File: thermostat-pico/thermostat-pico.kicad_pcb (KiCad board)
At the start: 2 copper layers, 40 x 30 mm, 22 parts, among them J1 VAC IN, J2 CTRL, J3 UART, U1 LY68L6400SLIT, U2 ESP32-PICO-D4, U3 LM358DR2G, U4 TPS5430DDA, U5 TPS5430DDA

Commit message: Should be finished
Maybe the antenna could be different
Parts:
- removed C4: 0.1uF/50V, Capacitor_SMD:C_0603_1608Metric
- added C10: 0.01uF, Capacitor_SMD:C_0402_1005Metric, F.Cu at (107.5, 99.0)
- added C8: 470uF/6.3V, Capacitor_Tantalum_SMD:CP_EIA-7343-31_Kemet-D, F.Cu at (118.0, 101.1)
- added C9: 470uF/6.3V, Capacitor_Tantalum_SMD:CP_EIA-7343-31_Kemet-D, F.Cu at (106.3, 103.5)
- added D2: SS34, Diode_SMD:D_SMA, F.Cu at (128.5, 105.2)
- added D3: SS34, Diode_SMD:D_SMA, F.Cu at (95.0, 112.5)
- added H1: MountingHole_Pad, MountingHole:MountingHole_2.2mm_M2_DIN965_Pad, F.Cu at (85.2, 114.2)
- added H2: MountingHole_Pad, MountingHole:MountingHole_2.2mm_M2_DIN965_Pad, F.Cu at (130.8, 88.8)
- added L1: 22uH, inductors:L_SXN_SMRH74-220MT, F.Cu at (127.5, 95.5)
- added L2: 22uH, inductors:L_SXN_SMRH74-220MT, F.Cu at (105.0, 110.5)
- added R10: 270, Resistor_SMD:R_0603_1608Metric, F.Cu at (114.5, 105.8)
- added R5: 10k, Resistor_SMD:R_0603_1608Metric, F.Cu at (100.0, 101.5)
- added R6: 10k, Resistor_SMD:R_0603_1608Metric, F.Cu at (114.5, 98.7)
- added R7: 1.1k, Resistor_SMD:R_0603_1608Metric, F.Cu at (96.5, 101.5)
- added R8: 5.6k, Resistor_SMD:R_0603_1608Metric, F.Cu at (114.5, 102.3)
- added R9: 33, Resistor_SMD:R_0603_1608Metric, F.Cu at (93.0, 101.5)
- AE1: value Antenna -> Antenna_Shield; footprint RF_Antenna:Texas_SWRA117D_2.4GHz_Right -> RF_Antenna:Texas_SWRA117D_2.4GHz_Left
- C3: value 0.1uF/50V -> 0.1uF; footprint Capacitor_SMD:C_0603_1608Metric -> Capacitor_SMD:C_0402_1005Metric
- C7: value 0.01uF -> 0.1uF
- JP1: moved to B.Cu
- moved J1 43.8 mm to (130.0, 113.5), turned to 180 degrees
- moved C2 31.9 mm to (123.5, 108.5)
- moved R1 27.2 mm to (91.5, 98.0), turned to -90 degrees
- moved J2 27.1 mm to (86.0, 105.2), turned to 90 degrees
- moved C6 26.8 mm to (130.0, 100.2), turned to 0 degrees
- moved D1 25.8 mm to (115.0, 112.5), turned to 180 degrees
- moved R2 23.5 mm to (91.5, 95.6), turned to 90 degrees
- moved U5 21.8 mm to (123.5, 103.5), turned to -90 degrees
- moved U3 20.8 mm to (96.5, 96.6)
- moved C3 16.2 mm to (100.5, 92.0), turned to 0 degrees
- moved R4 16.1 mm to (102.0, 93.7), turned to 90 degrees
- moved R3 13.5 mm to (102.0, 95.8), turned to 90 degrees
- moved J3 12.9 mm to (103.9, 87.5)
- moved U1 11.6 mm to (118.0, 92.0)
- moved U2 11.3 mm to (107.2, 93.5)
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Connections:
- net Net-(C5-Pad2) renamed /PH12
- net Net-(C6-Pad2) renamed /PH33
- AE1 pad 2: (no net) -> GND
- C1 pad 1: /REC_OUT -> /D1_OUT
- C2 pad 1: /REC_OUT -> /D1_OUT
- C3 pad 1: /REC_OUT -> GND
- C3 pad 2: GND -> /ADC1
- D1 pad 3: /REC_OUT -> /D1_OUT
- JP1 pad 1: unconnected-(JP1-Pad1) -> /BOOT
- JP1 pad 2: unconnected-(JP1-Pad2) -> GND
- R3 pad 2: Net-(R3-Pad2) -> /ADC1
- R4 pad 1: Net-(R3-Pad2) -> /ADC1
- U2 pad 1: Net-(U2-Pad1) -> /VCC33
- U2 pad 14: unconnected-(U2-Pad14) -> /DAC1
- U2 pad 15: unconnected-(U2-Pad15) -> /DAC2
- U2 pad 19: unconnected-(U2-Pad19) -> /VCC33
- U2 pad 23: unconnected-(U2-Pad23) -> /BOOT
- U2 pad 3: Net-(U2-Pad3) -> /VCC33
- U2 pad 37: unconnected-(U2-Pad37) -> /VCC33
- U2 pad 4: Net-(U2-Pad3) -> /VCC33
- U2 pad 43: Net-(U2-Pad1) -> /VCC33
- U2 pad 46: Net-(U2-Pad1) -> /VCC33
- U2 pad 5: unconnected-(U2-Pad5) -> /ADC1
- U2 pad 6: unconnected-(U2-Pad6) -> /ADC2
- U3 pad 3: unconnected-(U3-Pad3) -> /DAC1
- U3 pad 4: unconnected-(U3-Pad4) -> GND
- U3 pad 8: unconnected-(U3-Pad8) -> /VCC12
- U4 pad 4: unconnected-(U4-Pad4) -> Net-(R5-Pad2)
- U4 pad 7: /REC_OUT -> /D1_OUT
- U5 pad 4: unconnected-(U5-Pad4) -> Net-(R6-Pad2)
- U5 pad 7: /REC_OUT -> /D1_OUT
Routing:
- net GND: track 0.00 -> 60.1 mm, vias 0 -> 13
- net /VCC33: track 0.00 -> 55.2 mm, vias 0 -> 5
- net /D1_OUT: track 0.00 -> 25.5 mm, vias 0 -> 2
- net /BOOT: track 0.00 -> 16.0 mm, vias 0 -> 1
- net /VCC12: track 0.00 -> 15.0 mm, vias 0 -> 2
- net /CTRL0_IN: track 0.00 -> 14.4 mm
- net /DAC1: track 0.00 -> 11.7 mm
- net /CTRL0_OUT: track 0.00 -> 9.90 mm
- net Net-(R6-Pad2): track 0.00 -> 9.60 mm
- net Net-(R5-Pad2): track 0.00 -> 6.42 mm
- net /ADC1: track 0.00 -> 5.89 mm
- net /24VAC+: track 10.7 -> 5.37 mm
- net /24VAC-: track 9.08 -> 13.7 mm
- net Net-(C6-Pad1): track 0.00 -> 4.34 mm
- net Net-(R3-Pad1): track 0.00 -> 4.23 mm
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- added copper zone on B.Cu, net /D1_OUT
- added copper zone on F.Cu, net /PH12
- added copper zone on F.Cu, net /PH33
- added copper zone on F.Cu, net /VCC12
- added copper zone on F.Cu, net /VCC33
- added copper zone on B.Cu, net GND
- added copper zone on F.Cu, net GND
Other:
- board size 40 x 30 mm -> 50 x 30 mm
- board text added: "+"
- board text added: "-"
- board text added: "24VAC"
- board text added: "CTRL_IN"
- board text added: "CTRL_OUT"
- board text added: "GND"
- board text added: "URX"
- board text added: "UTX"
- board text added: "VCC"

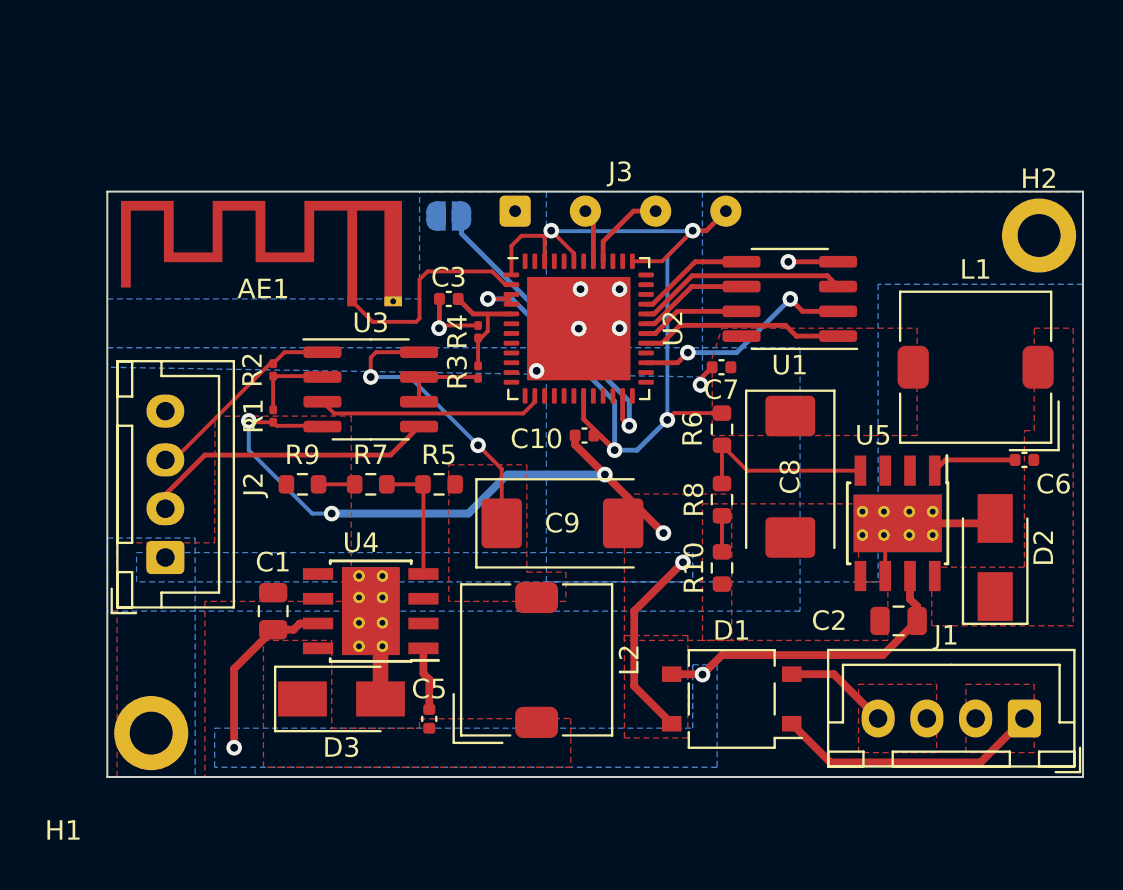
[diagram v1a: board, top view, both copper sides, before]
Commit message: Added slow start circuit
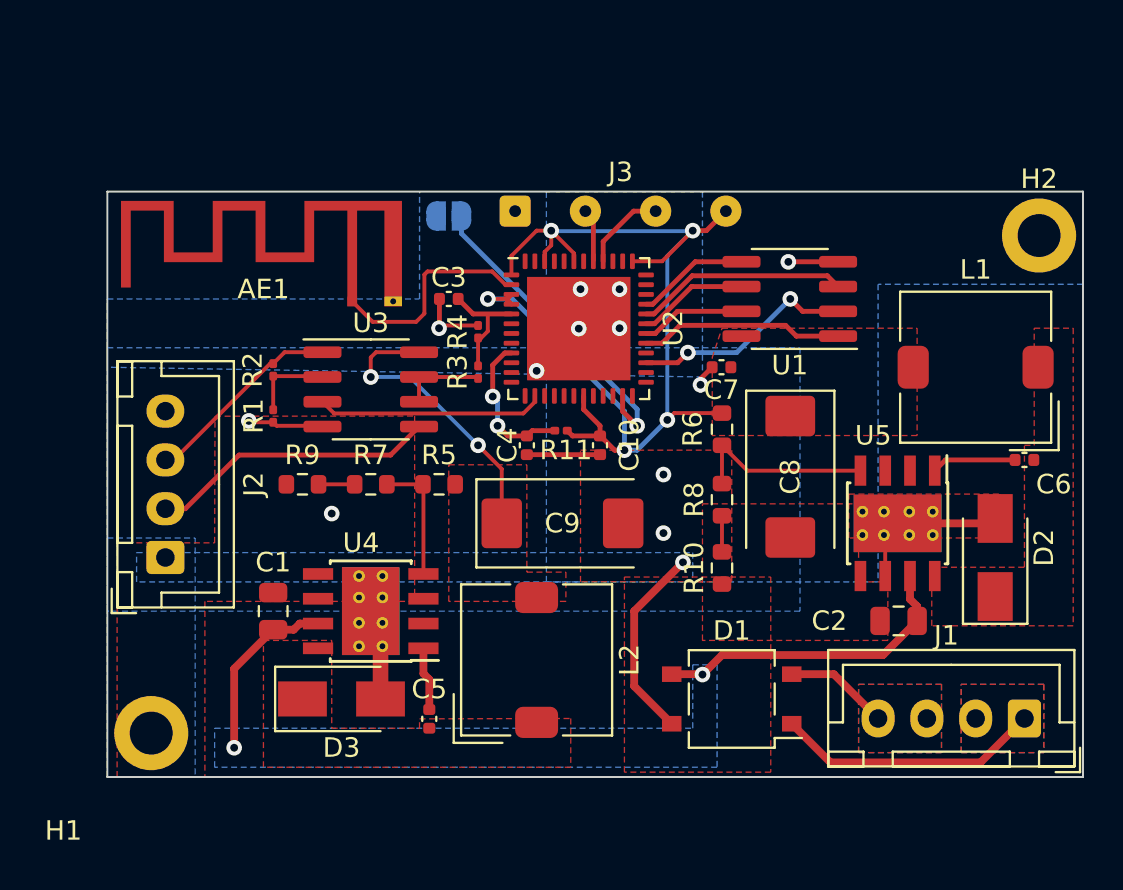
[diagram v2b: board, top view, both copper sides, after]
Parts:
- added C4: 1uF/5V, Capacitor_SMD:C_0402_1005Metric, F.Cu at (104.5, 99.5)
- added R11: 10k, Resistor_SMD:R_0201_0603Metric, F.Cu at (106.2, 98.8)
- moved C10 0.94 mm to (108.2, 99.5), turned to -90 degrees
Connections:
- U2 pad 9: unconnected-(U2-Pad9) -> /CHIP_PU
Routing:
- net GND: track 60.1 -> 34.7 mm
- net /CHIP_PU: track 0.00 -> 7.69 mm, vias 0 -> 2
- added copper zone on B.Cu, net /24VAC+
- added copper zone on B.Cu, net /24VAC-

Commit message: Add more connectors
And use a bigger op-amp. Surprised this fit.
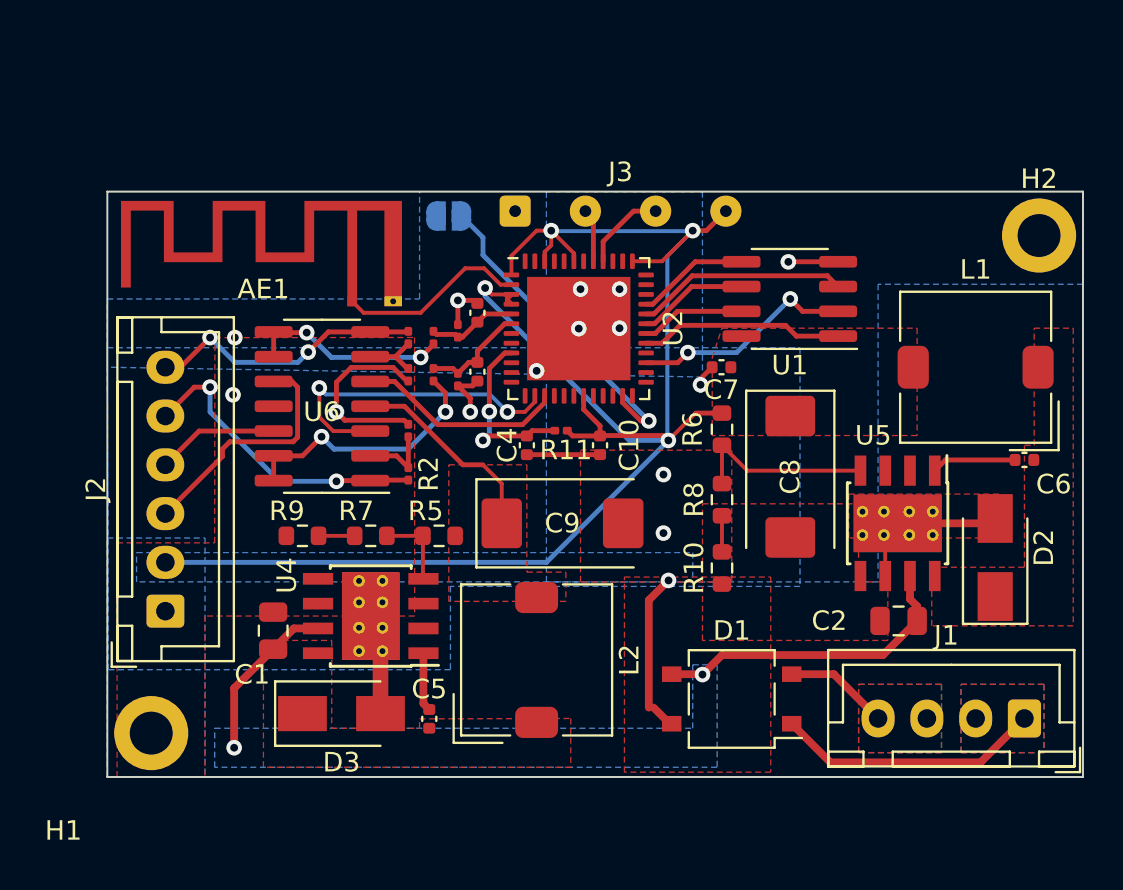
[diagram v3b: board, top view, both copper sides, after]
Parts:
- removed U3: LM358DR2G, Package_SO:SOIC-8_3.9x4.9mm_P1.27mm
- added C11: 0.1uF, Capacitor_SMD:C_0402_1005Metric, F.Cu at (102.0, 95.7)
- added R12: 33k, Resistor_SMD:R_0201_0603Metric, F.Cu at (98.4, 95.9)
- added R13: 68k, Resistor_SMD:R_0201_0603Metric, F.Cu at (98.4, 94.0)
- added R14: 18k, Resistor_SMD:R_0201_0603Metric, F.Cu at (99.7, 95.9)
- added R15: 2k, Resistor_SMD:R_0201_0603Metric, F.Cu at (101.0, 96.1)
- added U6: LM324DT, Package_SO:SOIC-14_3.9x8.7mm_P1.27mm, F.Cu at (94.0, 97.5)
- J2: value CTRL -> Conn_01x06; footprint Connector_JST:JST_XH_B4B-XH-A_1x04_P2.50mm_Vertical -> Connector_JST:JST_XH_B6B-XH-A_1x06_P2.50mm_Vertical
- moved R2 8.74 mm to (98.4, 101.0), turned to -90 degrees
- moved R1 6.96 mm to (98.4, 98.7), turned to 90 degrees
- moved R3 2.89 mm to (99.7, 94.0)
- moved J2 2.75 mm to (86.0, 108.0)
- moved R5 2.64 mm to (100.0, 104.1)
- moved R7 2.64 mm to (96.5, 104.1)
- moved R9 2.64 mm to (93.0, 104.1)
- moved C3 1.63 mm to (102.0, 92.7), turned to -90 degrees
- moved R4 1.04 mm to (101.0, 93.6)
- moved C1 1.00 mm to (91.5, 109.0)
- moved D3 0.75 mm to (95.0, 113.2)
- moved U4 0.25 mm to (96.5, 108.2)
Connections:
- J2 pad 2: /CTRL0_IN -> /VCC33
- J2 pad 3: /CTRL0_OUT -> /CTRL1_IN
- J2 pad 4: unconnected-(J2-Pad4) -> /CTRL2_IN
- R2 pad 2: /CTRL0_OUT -> /CTRL1_OUT
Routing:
- net /VCC33: track 55.6 -> 86.3 mm, vias 5 -> 4
- net /CTRL1_OUT: track 0.00 -> 15.8 mm, vias 0 -> 2
- net /CTRL0_IN: track 14.7 -> 0.00 mm
- net /CTRL2_OUT: track 0.00 -> 14.3 mm, vias 0 -> 2
- net Net-(R14-Pad1): track 0.00 -> 13.4 mm, vias 0 -> 2
- net /CTRL1_IN: track 0.00 -> 12.5 mm
- net /DAC2: track 0.00 -> 10.7 mm
- net /CTRL0_OUT: track 9.90 -> 0.00 mm
- net /CTRL2_IN: track 0.00 -> 6.27 mm
- net Net-(R3-Pad1): track 4.23 -> 10.3 mm, vias 0 -> 2
- net /ADC2: track 0.00 -> 5.49 mm
- net GND: track 34.7 -> 39.5 mm, vias 13 -> 15
- net /DAC1: track 11.7 -> 16.5 mm, vias 0 -> 2
- net /VCC12: track 15.0 -> 10.4 mm, vias 2 -> 0
- net Net-(R12-Pad1): track 0.00 -> 3.13 mm
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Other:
- board text added: "3V3"
- board text added: "CTRL1_IN"
- board text added: "CTRL1_OUT"
- board text added: "CTRL2_IN"
- board text added: "CTRL2_OUT"
- board text removed: "CTRL_IN"
- board text removed: "CTRL_OUT"

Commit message: Assembly updates
Apparently they can't do 0201 and need tooling holes
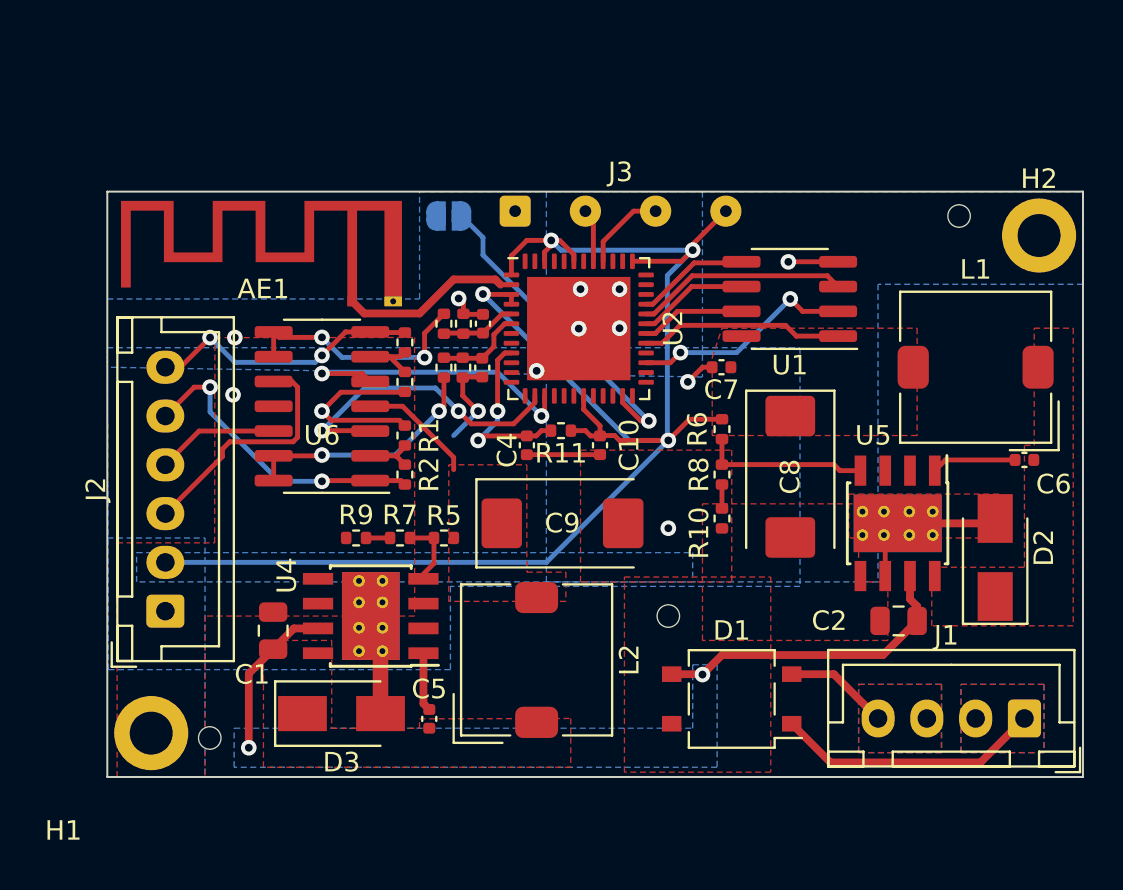
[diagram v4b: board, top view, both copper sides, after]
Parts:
- added H3: ToolingHole, kelvie:ToolingHole_1.152mm, F.Cu at (88.2, 114.5)
- added H4: ToolingHole, kelvie:ToolingHole_1.152mm, F.Cu at (126.7, 87.8)
- added H5: ToolingHole, kelvie:ToolingHole_1.152mm, F.Cu at (111.8, 108.2)
- R1, R11, R12, R13, R14, R15, R2, R3, R4: footprint Resistor_SMD:R_0201_0603Metric -> Resistor_SMD:R_0402_1005Metric
- R10, R5, R6, R7, R8, R9: footprint Resistor_SMD:R_0603_1608Metric -> Resistor_SMD:R_0402_1005Metric
- moved R9 2.75 mm to (95.8, 104.2)
- moved R10 2.54 mm to (114.5, 103.2)
- moved R7 1.50 mm to (98.0, 104.2)
- moved R8 1.29 mm to (114.5, 101.0)
- moved R3 0.89 mm to (100.2, 93.3), turned to -90 degrees
- moved R15 0.66 mm to (101.2, 95.5)
- moved R14 0.65 mm to (100.2, 95.5)
- moved C3 0.63 mm to (102.2, 93.3)
- moved R4 0.46 mm to (101.2, 93.3)
- moved R12 0.40 mm to (98.2, 96.2)
- moved C11 0.33 mm to (102.2, 95.5)
- moved R1 0.31 mm to (98.2, 99.0)
- moved R13 0.31 mm to (98.2, 94.2)
- moved R5 0.27 mm to (100.2, 104.2)
- moved R2 0.18 mm to (98.2, 101.0)
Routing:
- net GND: track 39.5 -> 33.5 mm, vias 15 -> 13
- net /DAC2: track 10.7 -> 16.0 mm, vias 0 -> 2
- net /VCC12: track 10.4 -> 5.99 mm
- net /VCC33: track 86.3 -> 83.8 mm
- net Net-(R3-Pad1): track 10.3 -> 12.0 mm
- net Net-(R1-Pad1): track 3.78 -> 2.68 mm
- net Net-(R6-Pad2): track 9.60 -> 8.53 mm
- net /ADC2: track 5.49 -> 4.57 mm
- net Net-(R14-Pad1): track 13.4 -> 12.5 mm
- net Net-(R12-Pad1): track 3.13 -> 3.96 mm
- net /ADC1: track 4.61 -> 3.88 mm
- net /DAC1: track 16.5 -> 15.9 mm
- net Net-(R10-Pad2): track 1.85 -> 1.23 mm
- net Net-(R7-Pad1): track 1.85 -> 1.23 mm

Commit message: Update tracks, add inductor 3D model
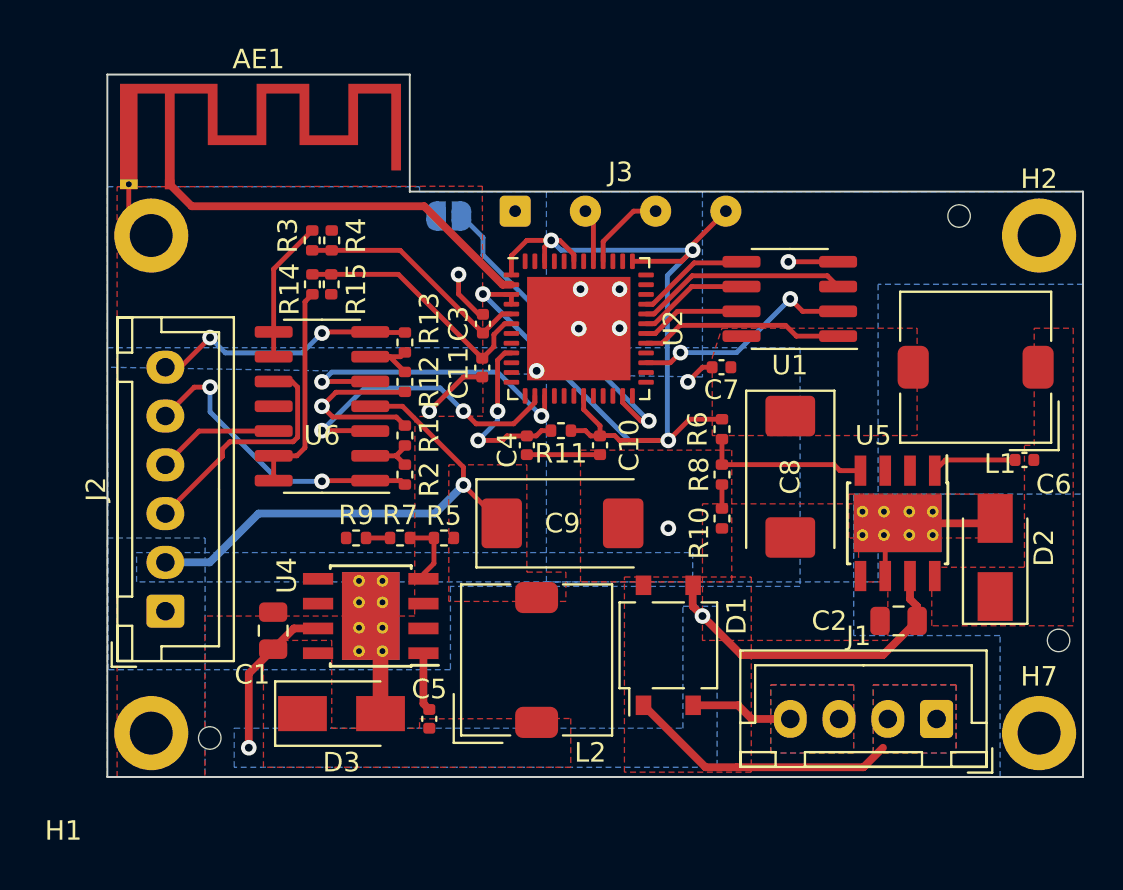
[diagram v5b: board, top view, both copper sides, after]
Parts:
- added H6: Hole, MountingHole:MountingHole_2.2mm_M2_DIN965_Pad, F.Cu at (85.2, 88.8)
- added H7: Hole, MountingHole:MountingHole_2.2mm_M2_DIN965_Pad, F.Cu at (130.8, 114.2)
- AE1: footprint RF_Antenna:Texas_SWRA117D_2.4GHz_Left -> kelvie:Texas_SWRA117D_2.4GHz_Right
- H1, H2: value MountingHole_Pad -> Hole
- moved H5 20.0 mm to (131.8, 109.5)
- moved AE1 11.1 mm to (86.2, 86.1)
- moved R3 7.99 mm to (93.5, 89.0)
- moved R4 7.99 mm to (94.5, 89.0)
- moved R15 7.98 mm to (94.5, 91.2)
- moved R14 7.98 mm to (93.5, 91.2)
- moved J1 4.50 mm to (125.5, 113.5)
- moved D1 4.26 mm to (111.8, 109.8), turned to 90 degrees
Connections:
- J2 pad 2: /VCC33 -> /VCC12
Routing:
- net /VCC33: track 83.8 -> 55.5 mm
- net /VCC12: track 5.99 -> 26.7 mm, vias 0 -> 1
- net Net-(AE1-Pad1): track 9.25 -> 19.6 mm
- net /ADC2: track 4.57 -> 13.1 mm
- net /ADC1: track 3.88 -> 12.4 mm
- net Net-(R3-Pad1): track 12.0 -> 7.29 mm, vias 2 -> 0
- net Net-(R14-Pad1): track 12.5 -> 11.1 mm, vias 2 -> 0
- net GND: track 33.5 -> 34.3 mm, vias 13 -> 11
- net /D1_OUT: track 24.5 -> 25.1 mm
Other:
- board size 50 x 30 mm -> 50 x 36 mm
- board text added: "12VDC"
- board text removed: "VCC"
